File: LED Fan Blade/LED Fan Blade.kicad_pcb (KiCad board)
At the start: 4 copper layers, 177.3 x 138.2 mm, 64 parts

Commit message: Finished up PCB
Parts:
- added Boot1: SW_Push, FanbladeFootprints:ButtonSMD, F.Cu at (138.3, 115.8)
- added C4: 47pF, Capacitor_SMD:C_0201_0603Metric, F.Cu at (154.9, 124.0)
- added CB1: 100nF, Capacitor_SMD:C_0201_0603Metric, F.Cu at (153.5, 116.8)
- added Cin1: 10uF, Capacitor_SMD:C_0201_0603Metric, F.Cu at (159.5, 119.5)
- added Cout1: 47uF, Capacitor_SMD:C_0201_0603Metric, F.Cu at (151.8, 118.5)
- added HallSensor1: MRMS201A-001, FanbladeFootprints:XDCR_MRMS201A-001, F.Cu at (59.1, 25.1)
- added L1: 2.4uH, Inductor_SMD:L_0201_0603Metric, F.Cu at (153.9, 115.4)
- added Power_12V1: Power Terminal, FanbladeFootprints:Power_Terminal, F.Cu at (162.5, 127.8)
- added R7: 100K, Resistor_SMD:R_0201_0603Metric, F.Cu at (154.0, 122.4)
- added R8: 21.5k, Resistor_SMD:R_0201_0603Metric, F.Cu at (156.0, 122.4)
- added R9: 5.11K, Resistor_SMD:R_0201_0603Metric, F.Cu at (170.7, 110.9)
- added VReg1: ~, FanbladeFootprints:AN_SY8105, F.Cu at (155.8, 118.8)
- BL:0, BL:1, BL:2, BL:3, BL:4, BL:5: value 10K -> 5 Ω
- GR:0, GR:1, GR:2, GR:3, GR:4, GR:5: value 10K -> 15 Ω
- RD:0, RD:1, RD:2, RD:3, RD:4, RD:5: value 10K -> 65 Ω
- moved R4 29.0 mm to (176.4, 111.0)
- moved R3 28.9 mm to (173.1, 110.9)
- moved R1 28.3 mm to (179.8, 112.5)
- moved USB-C1 28.3 mm to (174.0, 118.6)
- moved R2 15.8 mm to (138.4, 111.3), turned to 0 degrees
- moved GR:4 2.06 mm to (116.2, 96.8)
- moved GR:5 1.68 mm to (122.4, 93.7)
- moved RD:5 1.19 mm to (118.7, 96.0)
- moved VCAP1 1.18 mm to (119.4, 80.3)
- moved GR:2 1.15 mm to (96.6, 68.5)
- moved R6 1.07 mm to (120.5, 78.5)
- moved GR:3 1.02 mm to (107.6, 90.7)
- moved RD:3 0.89 mm to (107.7, 85.2)
- moved BL:4 0.85 mm to (114.2, 95.5)
- moved RD:4 0.77 mm to (112.5, 94.2)
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- renumbered CapVCAP1 to VCAP1
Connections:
- ESP1 pad 15: unconnected-(ESP1-IO3-Pad15) -> Hall Sense
- ESP1 pad 2: Net-(ESP1-EN) -> +3.3V
- ESP1 pad 8: unconnected-(ESP1-IO9-Pad8) -> Net-(ESP1-IO9)
- LED-Driver1 pad 16: +5V -> +3.3V
- LED-Driver1 pad 40: +5V -> +3.3V
- R2 pad 1: +3.3V -> GND
- R2 pad 2: Net-(ESP1-EN) -> Net-(Boot1-Pad2)
- USB-C1 pad A4: unconnected-(USB-C1-VBUS-PadA4) -> Net-(R9-Pad2)
- USB-C1 pad A9: unconnected-(USB-C1-VBUS-PadA4) -> Net-(R9-Pad2)
- USB-C1 pad B4: unconnected-(USB-C1-VBUS-PadA4) -> Net-(R9-Pad2)
- USB-C1 pad B9: unconnected-(USB-C1-VBUS-PadA4) -> Net-(R9-Pad2)
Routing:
- net Hall Sense: track 0.00 -> 149.4 mm, vias 0 -> 2
- net +3.3V: track 0.00 -> 48.7 mm, vias 0 -> 7
- net +12V: track 0.00 -> 25.0 mm
- net GND: track 42.6 -> 66.2 mm, vias 3 -> 6
- net Net-(ESP1-IO9): track 0.00 -> 12.4 mm
- net Net-(R9-Pad2): track 0.00 -> 11.1 mm
- net Net-(Boot1-Pad2): track 0.00 -> 11.0 mm
- net CS17: track 40.2 -> 47.8 mm
- net D+: track 37.3 -> 31.1 mm
- net Net-(VReg1-LX): track 0.00 -> 5.75 mm
- net Net-(VReg1-FB): track 0.00 -> 5.54 mm
- net CS8: track 42.4 -> 47.9 mm
- net CS2: track 83.9 -> 89.1 mm
- net Net-(ESP1-EN): track 4.75 -> 0.00 mm
- net CS11: track 30.9 -> 35.4 mm
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- added copper zone on In2.Cu, net +3.3V
- removed copper zone on In2.Cu, net +5V
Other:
- outline, holes or cut-outs redrawn

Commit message: Changed PCB
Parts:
- BL:0, BL:1, BL:2, BL:3, BL:4, BL:5: value 5 Ω -> 5; footprint Resistor_SMD:R_0201_0603Metric -> FanbladeFootprints:Resistor_603
- C4, CB1, Cin1, Cout1, VCAP1: footprint Capacitor_SMD:C_0201_0603Metric -> FanbladeFootprints:Cap_603
- GR:0, GR:1, GR:2, GR:3, GR:4, GR:5: value 15 Ω -> 15; footprint Resistor_SMD:R_0201_0603Metric -> FanbladeFootprints:Resistor_603
- L1: footprint Inductor_SMD:L_0201_0603Metric -> FanbladeFootprints:Inductor_Sunlord
- R1, R2, R3, R4, R5, R6, R7, R8, R9: footprint Resistor_SMD:R_0201_0603Metric -> FanbladeFootprints:Resistor_603
- RD:0, RD:1, RD:2, RD:3, RD:4, RD:5: value 65 Ω -> 65; footprint Resistor_SMD:R_0201_0603Metric -> FanbladeFootprints:Resistor_603
- moved L1 2.93 mm to (154.8, 112.6)
- moved R7 2.67 mm to (151.6, 123.6)
- moved C4 1.59 mm to (155.7, 125.3)
- moved Cout1 1.48 mm to (150.5, 117.7)
- moved CB1 0.51 mm to (153.0, 116.8)
- moved VCAP1 0.51 mm to (119.4, 80.8)
- moved R3 0.40 mm to (172.7, 110.7)
- moved R5 0.22 mm to (131.4, 105.5)
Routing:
- net +3.3V: track 48.7 -> 56.0 mm
- net Net-(VReg1-FB): track 5.54 -> 11.6 mm
- net Net-(VReg1-LX): track 5.75 -> 11.7 mm
- net +12V: track 25.0 -> 23.7 mm
- net Net-(USB-C1-CC1): track 2.49 -> 1.57 mm
- net GND: track 66.2 -> 65.4 mm

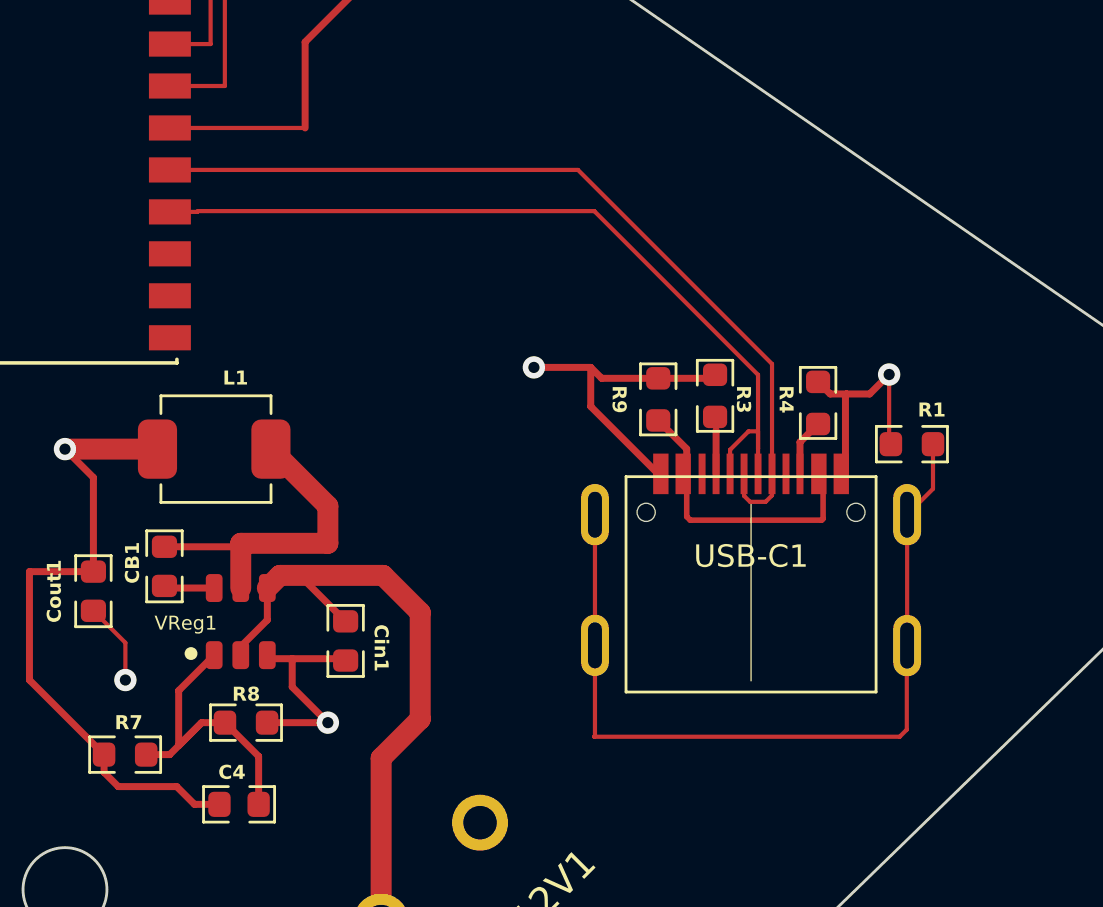
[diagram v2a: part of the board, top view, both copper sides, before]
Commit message: Changed USB C connector to different one
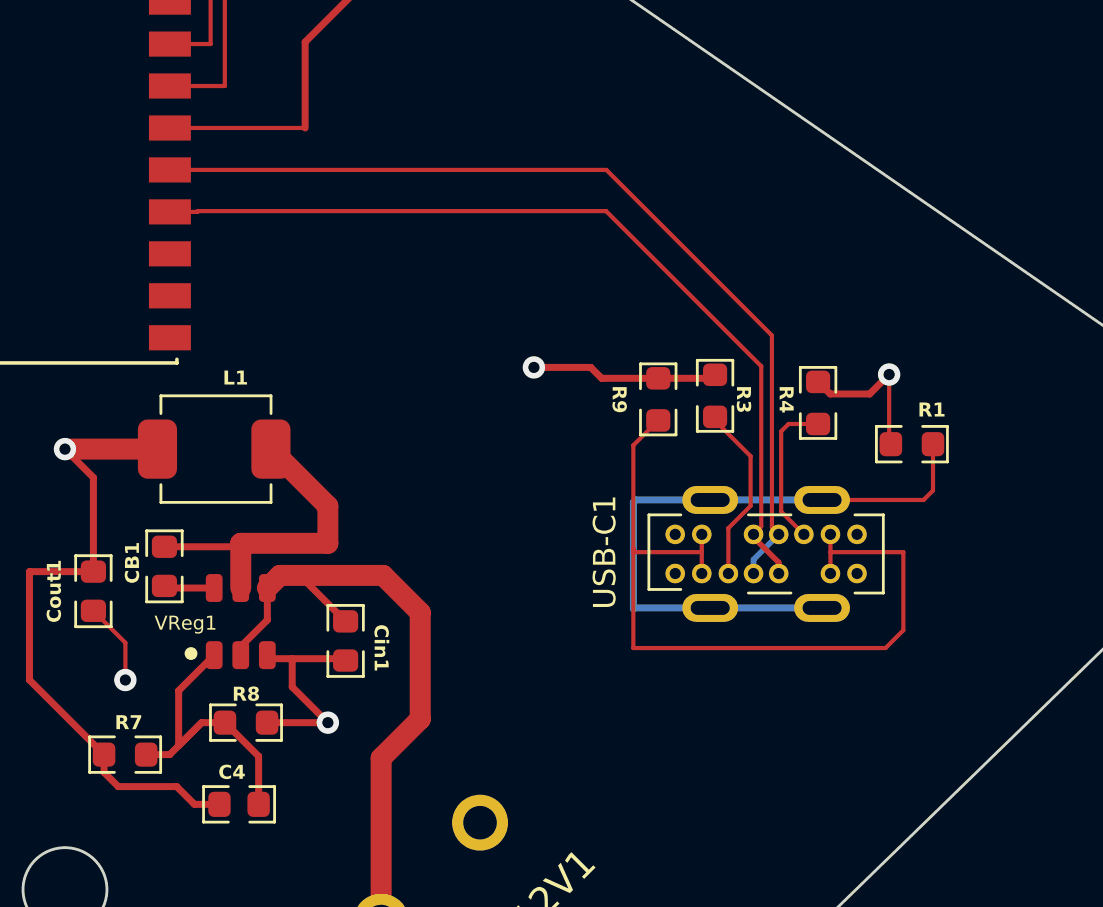
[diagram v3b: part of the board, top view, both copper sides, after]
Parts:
- moved USB-C1 40.3 mm to (153.1, 84.1), turned to -90 degrees
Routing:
- net Net-(R9-Pad2): track 10.7 -> 29.2 mm
- net GND: track 65.4 -> 57.8 mm
- net Net-(USB-C1-SHIELD): track 29.8 -> 23.1 mm
- net Net-(USB-C1-CC1): track 1.57 -> 6.46 mm
- net Net-(USB-C1-CC2): track 2.05 -> 5.45 mm
- net D+: track 31.1 -> 33.0 mm
- net D-: track 29.8 -> 31.3 mm
